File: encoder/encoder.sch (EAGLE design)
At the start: 17 parts, among them SW1 EC12E_SW, U1 SN74LVC1G14DBVRDBV5-L, U2 SN74LVC1G14DBVRDBV5-L, U3 SN74LVC1G14DBVRDBV5-L

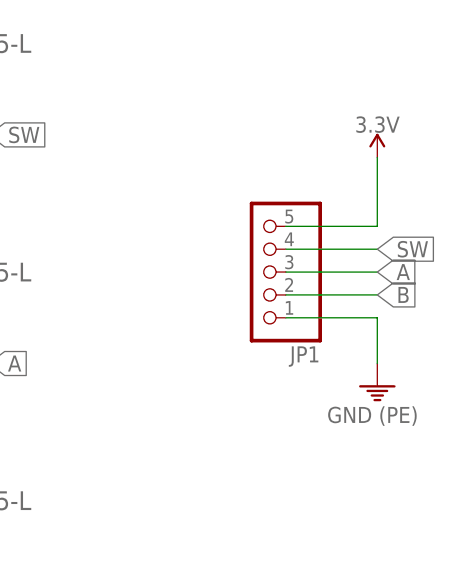
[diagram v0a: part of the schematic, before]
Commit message: Added SD breakout
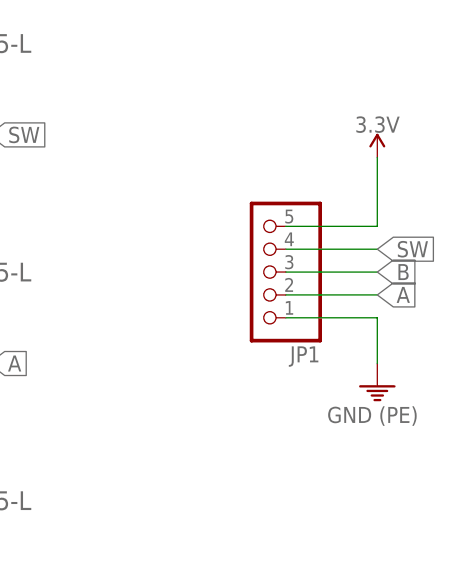
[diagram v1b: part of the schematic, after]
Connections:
- net A: now also JP1.2; no longer JP1.3
- net B: now also JP1.3; no longer JP1.2
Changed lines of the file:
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@@
 </segment>
 <segment>
-<pinref part="JP1" gate="A" pin="3"/>
-<wire x1="116.84" y1="0" x2="127" y2="0" width="0.1524" layer="91"/>
-<label x="127" y="0" size="1.778" layer="95" xref="yes"/>
+<pinref part="JP1" gate="A" pin="2"/>
+<wire x1="116.84" y1="-2.54" x2="127" y2="-2.54" width="0.1524" layer="91"/>
+<label x="127" y="-2.54" size="1.778" layer="95" xref="yes"/>
 </segment>
 </net>
@@
 </segment>
 <segment>
-<pinref part="JP1" gate="A" pin="2"/>
-<wire x1="116.84" y1="-2.54" x2="127" y2="-2.54" width="0.1524" layer="91"/>
-<label x="127" y="-2.54" size="1.778" layer="95" xref="yes"/>
+<pinref part="JP1" gate="A" pin="3"/>
+<wire x1="116.84" y1="0" x2="127" y2="0" width="0.1524" layer="91"/>
+<label x="127" y="0" size="1.778" layer="95" xref="yes"/>
 </segment>
 </net>
